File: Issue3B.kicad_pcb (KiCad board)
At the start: 2 copper layers, 213.1 x 129 mm, 206 parts, among them IC1 ULA, IC10 4116, IC11 4116, IC12 4116, IC13 4116, IC14 LM1889, IC15 4532, IC16 4532, IC17 4532, IC18 4532, IC19 4532, IC2 Z80, IC20 4532, IC21 4532, IC22 4532, IC23 LS32, IC24 LS00, IC25 LS157, IC26 LS157, IC3 LS157, IC4 LS157, IC5 ROM, IC6 4116, IC7 4116, IC8 4116, IC9 4116, J7 Barrel_Jack_MountingPin, T1 Transformer_1P_1S, X1 14Mhz, X2 4.43Mhz

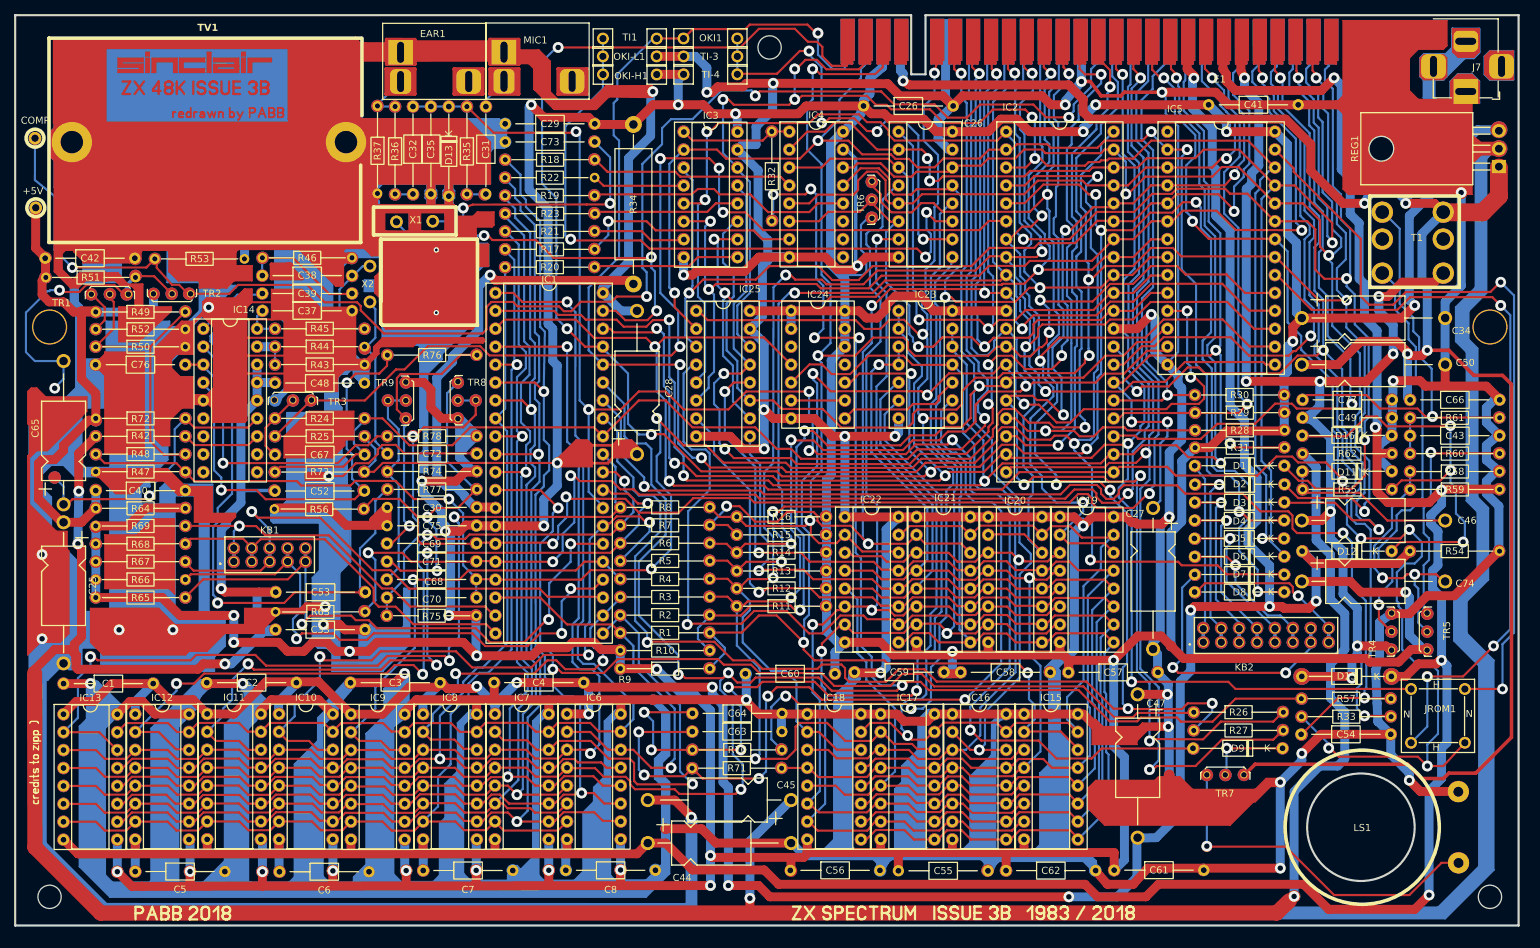
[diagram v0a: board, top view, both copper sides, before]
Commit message: Updated for PCB size and hole positions
Updated for PCB size and hole positions.
Also included stp file for the component models.
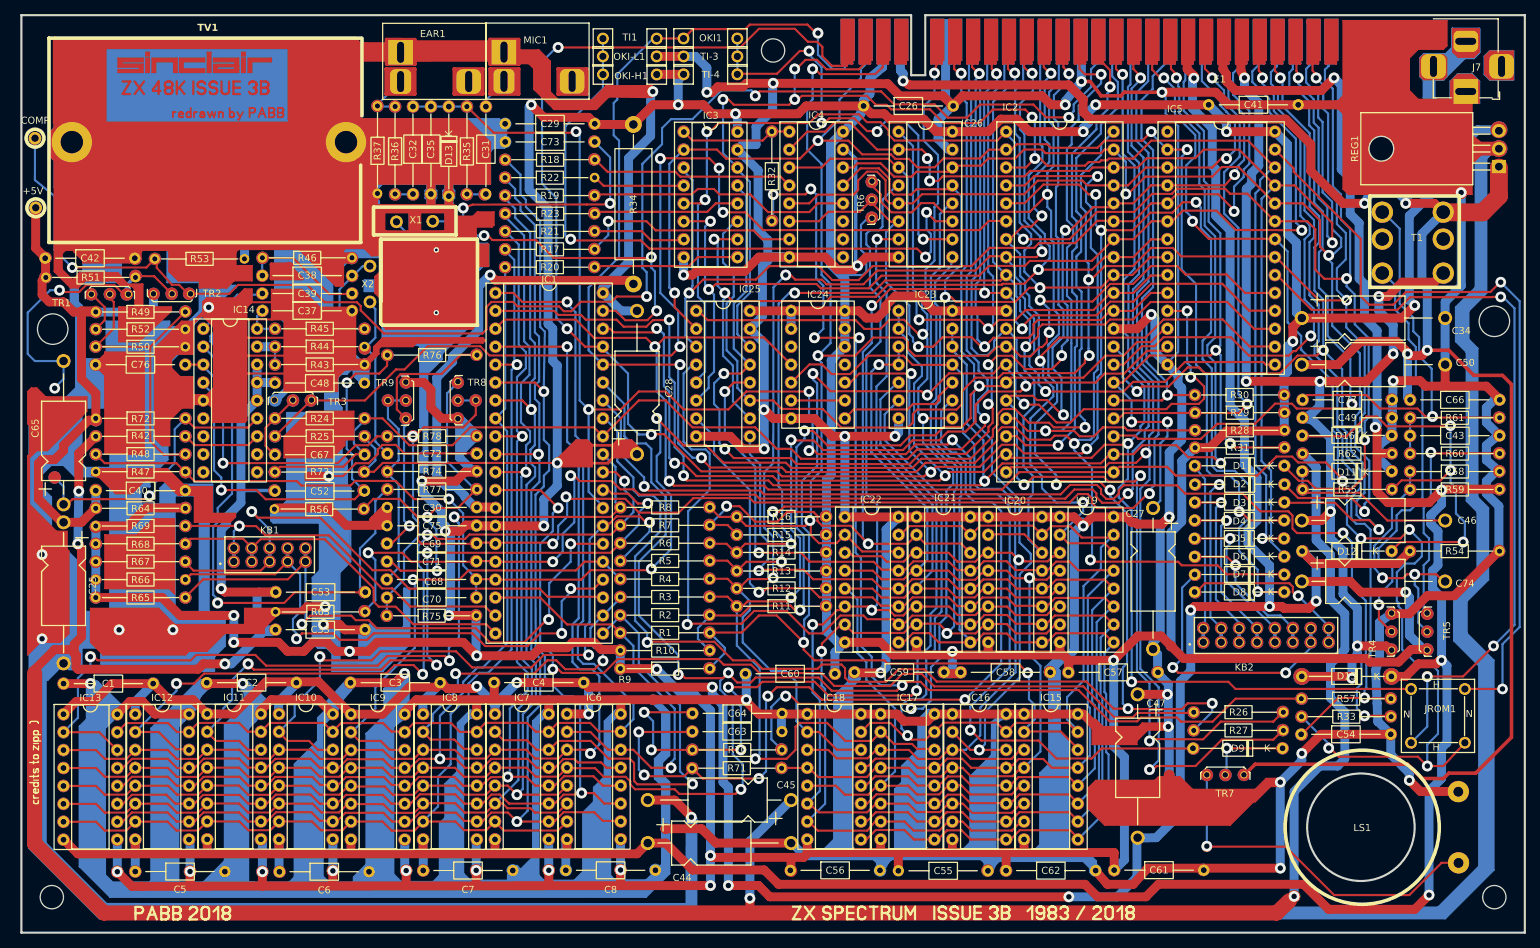
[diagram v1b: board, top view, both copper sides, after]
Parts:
- removed LL1, LR1, TM1: MountingHole, Mod:MountingHole_3.3mm Spectrum
- removed LM1, RM1: MountingHole, Mod:MountingHole_5mm Spectrum
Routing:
- net Net-(IC5-CS): track 106.6 -> 108.1 mm
- net Net-(IC5-OE1L): track 111.9 -> 112.6 mm
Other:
- board size 213.1 x 129 mm -> 213.1 x 130 mm
